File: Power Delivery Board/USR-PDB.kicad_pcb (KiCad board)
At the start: 2 copper layers, 110 x 150 mm, 40 parts, among them IC1 LM7805ECT, IC2 LM7805ECT, J1 XT90PW-M, U10 Anderson PP45 Vert. 2x1, U11 Anderson PP45 Vert. 2x1, U12 Anderson PP45 Vert. 2x1, U14 MCP3002-I/P, U17 AMS1117-3.3, U2 Anderson PP45 Vert. 2x1, U3 Anderson PP45 Vert. 2x1, U4 Anderson PP45 Vert. 2x1, U5 Anderson PP45 Vert. 2x1, U6 Anderson PP45 Vert. 2x1, U7 LM2676T-12_NOPB

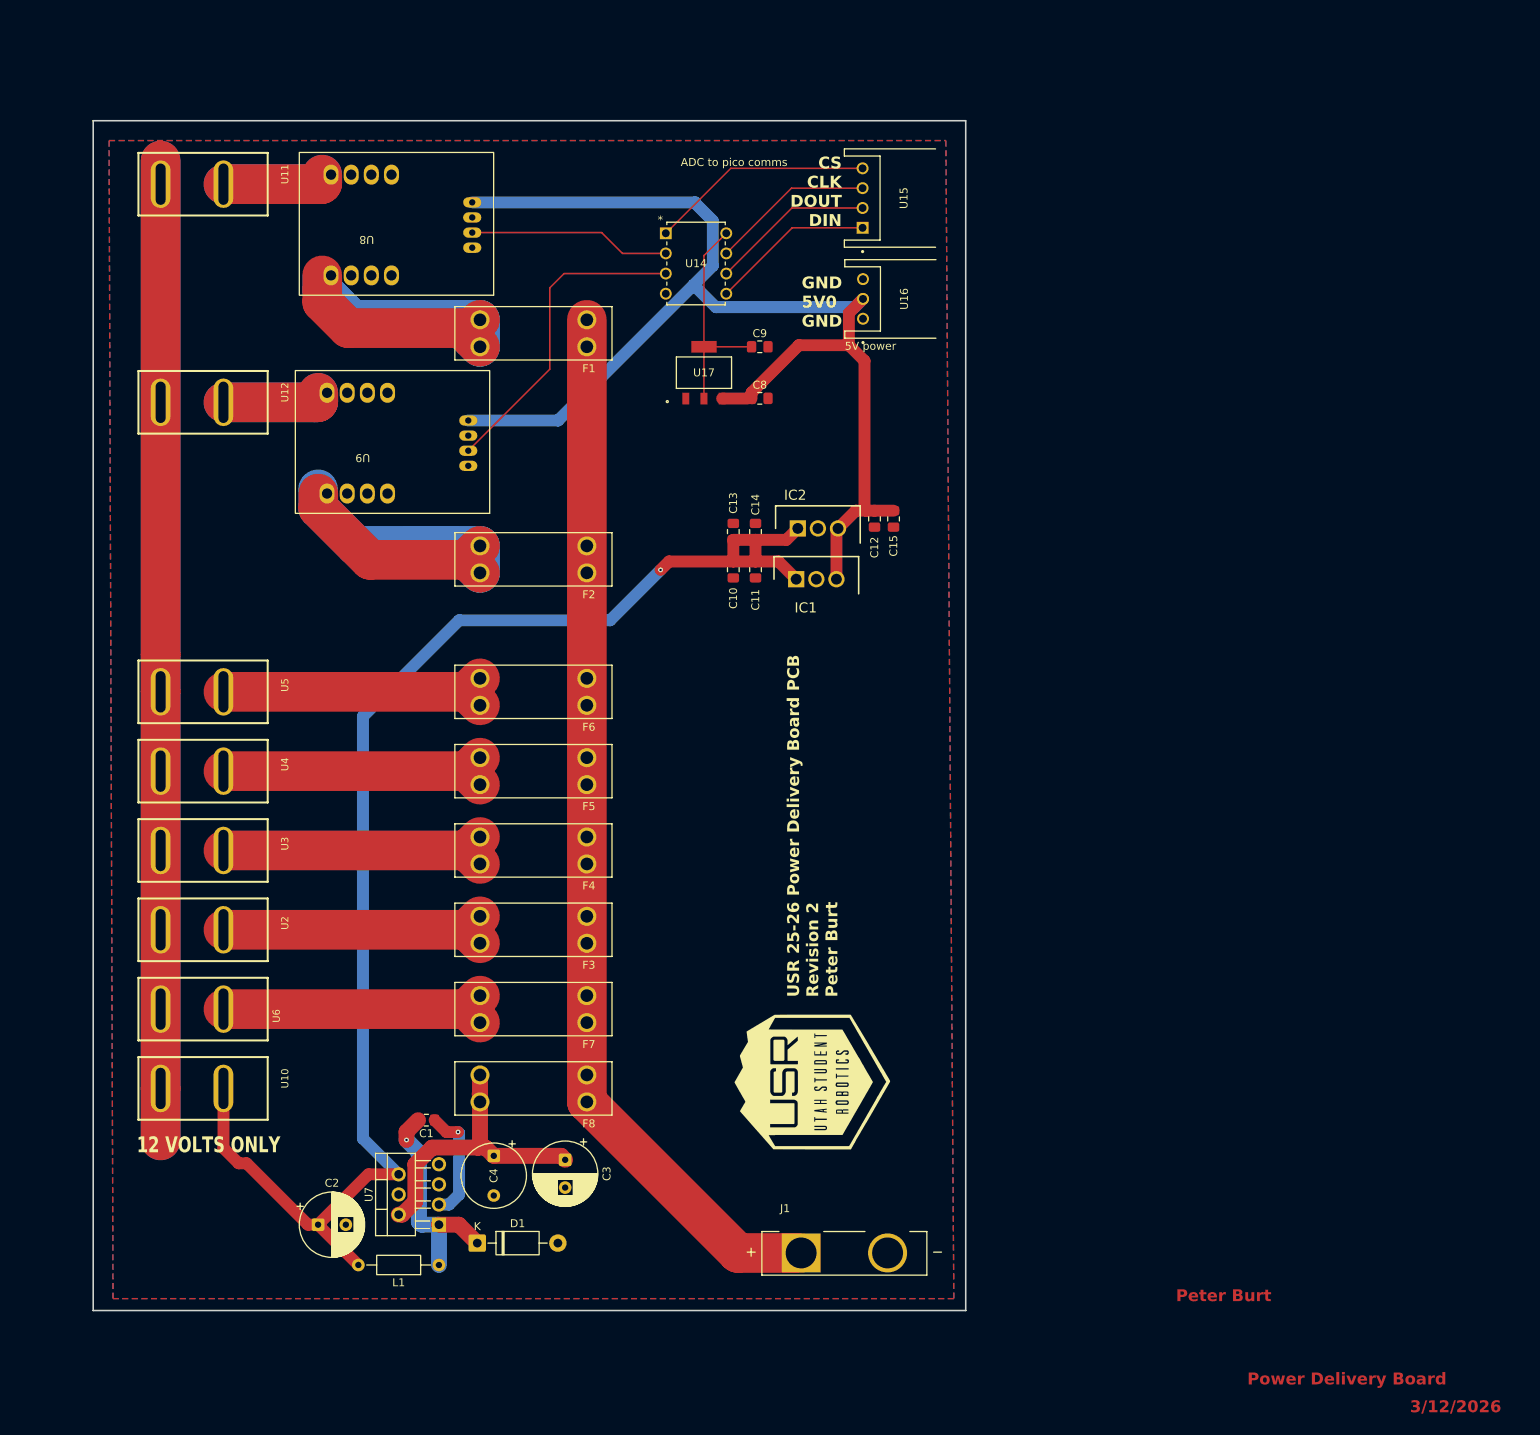
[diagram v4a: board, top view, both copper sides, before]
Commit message: updated trace widths for HE sensors
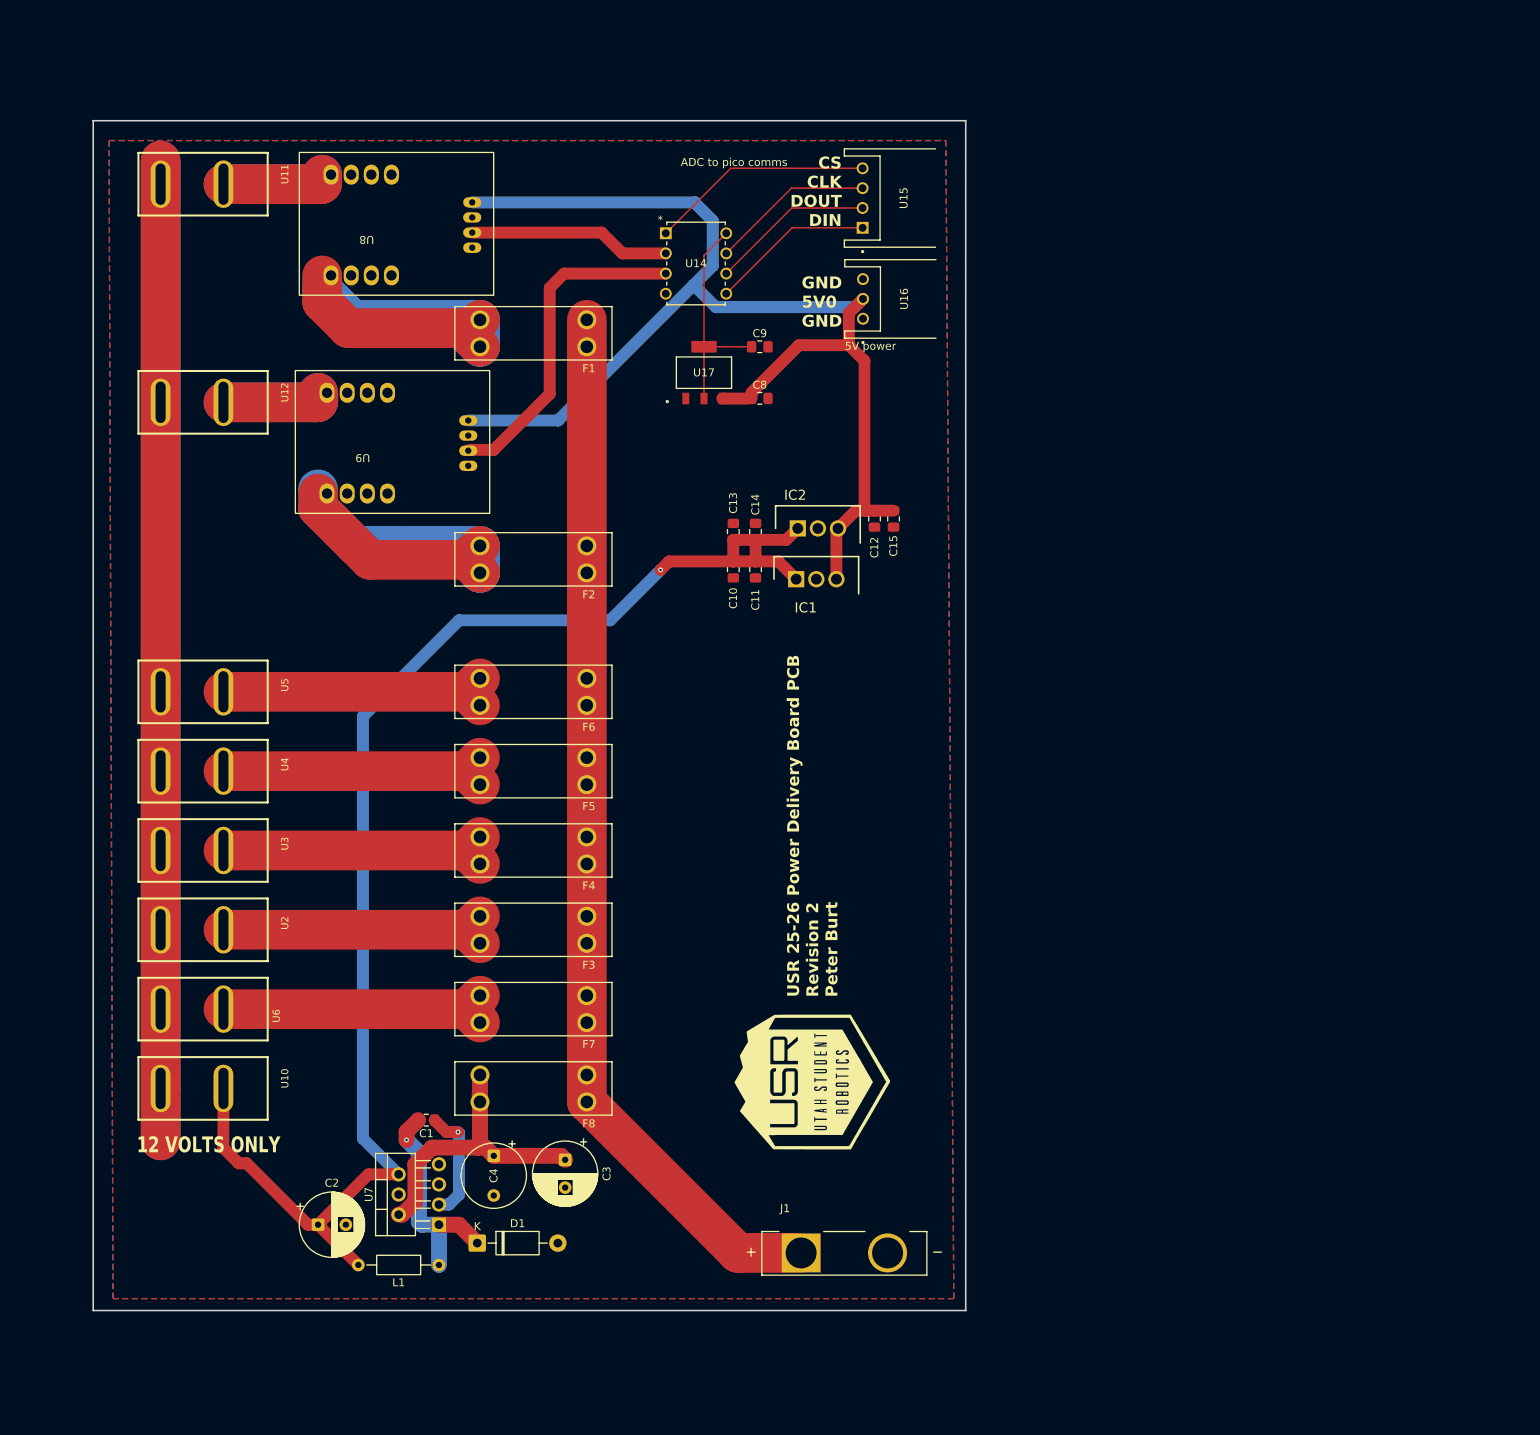
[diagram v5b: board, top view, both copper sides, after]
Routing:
- net HE2_out: track 40.2 -> 42.0 mm
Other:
- board text removed: "3/12/2026"
- board text removed: "Peter Burt"
- board text removed: "Power Delivery Board"
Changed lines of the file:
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@@
 	)
 	(paper "A4")
+	(title_block
+		(title "Power Delivery Board 2025-2026")
+		(date "2026-03-26")
+		(company "Utah Student Robotics")
+		(comment 1 "Peter Burt ")
+	)
 	(layers
 		(0 "F.Cu" signal)
@@
 		(layer "Edge.Cuts")
 	)
-	(gr_text "Peter Burt\n"
-		(at 178 180 0)
-		(layer "F.Cu")
-		(effects
-			(font
-				(size 1.5 1.5)
-				(thickness 0.3)
-				(bold yes)
-			)
-			(justify left bottom)
-		)
-	)
-	(gr_text "Power Delivery Board\n"
-		(at 187 190.5 0)
-		(layer "F.Cu")
-		(effects
-			(font
-				(size 1.5 1.5)
-				(thickness 0.3)
-				(bold yes)
-			)
-			(justify left bottom)
-		)
-	)
-	(gr_text "3/12/2026\n"
-		(at 207.5 194 0)
-		(layer "F.Cu")
-		(effects
-			(font
-				(size 1.5 1.5)
-				(thickness 0.3)
-				(bold yes)
-			)
-			(justify left bottom)
-		)
-	)
 	(gr_text "ADC to pico comms"
 		(at 115.57 36.83 0)
@@
 		(start 100.86 50.27)
 		(end 113.69 50.27)
-		(width 0.2)
+		(width 1.5)
 		(layer "F.Cu")
 		(net "HE2_out")
@@
 		(start 99.06 52.07)
 		(end 100.86 50.27)
-		(width 0.2)
+		(width 1.5)
 		(layer "F.Cu")
 		(net "HE2_out")
 	)
 	(segment
-		(start 88.785 72.6025)
-		(end 99.06 62.3275)
-		(width 0.2)
+		(start 88.8875 72.5)
+		(end 92 72.5)
+		(width 1.5)
 		(layer "F.Cu")
 		(net "HE2_out")
 	)
 	(segment
-		(start 99.06 62.3275)
+		(start 92 72.5)
+		(end 99.06 65.44)
+		(width 1.5)
+		(layer "F.Cu")
+		(net "HE2_out")
+	)
+	(segment
+		(start 99.06 65.44)
 		(end 99.06 52.07)
+		(width 1.5)
+		(layer "F.Cu")
+		(net "HE2_out")
+	)
+	(segment
+		(start 88.785 72.6025)
+		(end 88.8875 72.5)
 		(width 0.2)
 		(layer "F.Cu")
@@
 		(start 89.285 45.1025)
 		(end 105.6025 45.1025)
-		(width 0.2)
+		(width 1.5)
 		(layer "F.Cu")
 		(net "HE1_out")
@@
 		(start 108.23 47.73)
 		(end 113.69 47.73)
-		(width 0.2)
+		(width 1.5)
 		(layer "F.Cu")
 		(net "HE1_out")
@@
 		(start 105.6025 45.1025)
 		(end 108.23 47.73)
-		(width 0.2)
+		(width 1.5)
 		(layer "F.Cu")
 		(net "HE1_out")

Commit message: Added vias to PDB to stitch together front and back ground planes
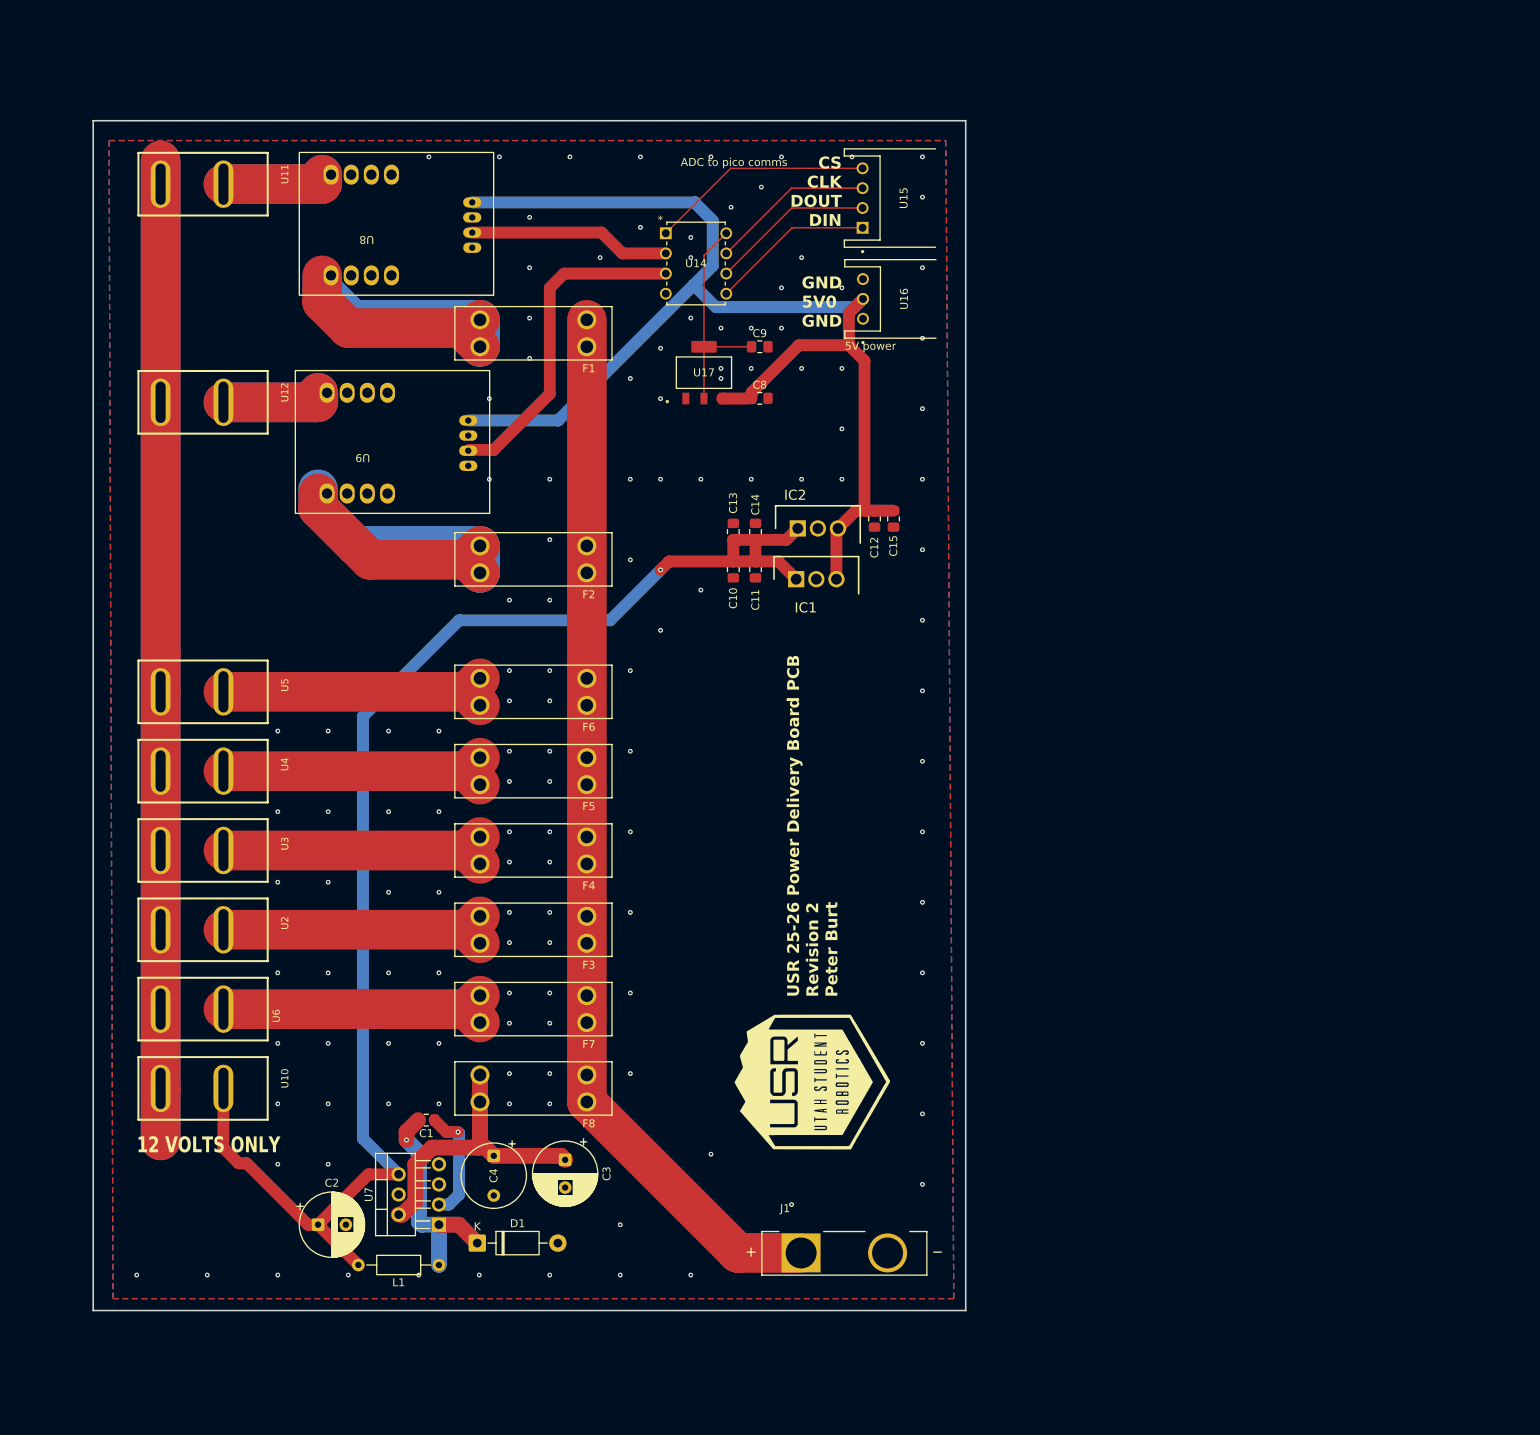
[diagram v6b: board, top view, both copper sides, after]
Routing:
- net GND: vias 0 -> 132

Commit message: generated gerbers for all remaining pcbs
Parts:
- added REF**: MountingHole_3.2mm_M3_DIN965_Pad_TopBottom, MountingHole:MountingHole_3.2mm_M3_DIN965_Pad_TopBottom, F.Cu at (132.1, 71.1)
- added REF**: MountingHole_3.2mm_M3_DIN965_Pad_TopBottom, MountingHole:MountingHole_3.2mm_M3_DIN965_Pad_TopBottom, F.Cu at (59.7, 53.3)
- added REF**: MountingHole_3.2mm_M3_DIN965_Pad_TopBottom, MountingHole:MountingHole_3.2mm_M3_DIN965_Pad_TopBottom, F.Cu at (49.5, 172.7)
- added REF**: MountingHole_3.2mm_M3_DIN965_Pad_TopBottom, MountingHole:MountingHole_3.2mm_M3_DIN965_Pad_TopBottom, F.Cu at (109.2, 172.7)

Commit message: Complete redesign of PDB pcb
AAAAAAAAAAAAAAAAAAAAAAAAAAAAAAAAAAAAAAAAAAAA
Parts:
- removed the REF** at (132.1, 71.1)
- removed the REF** at (59.7, 53.3)
- removed the REF** at (49.5, 172.7)
- removed the REF** at (109.2, 172.7)
- added G***: LOGO, LOGO, F.Cu at (104.1, 40.6)
- added REF**: MountingHole_3.2mm_M3_Pad_Via, MountingHole:MountingHole_3.2mm_M3_Pad_Via, F.Cu at (37.0, 23.0)
- added REF**: MountingHole_3.2mm_M3_Pad_Via, MountingHole:MountingHole_3.2mm_M3_Pad_Via, F.Cu at (115.4, 181.5)
- added REF**: MountingHole_3.2mm_M3_Pad_Via, MountingHole:MountingHole_3.2mm_M3_Pad_Via, F.Cu at (37.0, 181.5)
- added REF**: MountingHole_3.2mm_M3_Pad_Via, MountingHole:MountingHole_3.2mm_M3_Pad_Via, F.Cu at (115.4, 23.0)
- C1, C10, C11, C12, C13, C14, C15, C8, C9, U17: moved to B.Cu
- C4: footprint Capacitor_THT:CP_Radial_Tantal_D8.0mm_P5.00mm -> Capacitor_THT:CP_Radial_D10.0mm_P5.00mm
- moved J1 159.8 mm to (77.5, 25.4), turned to 180 degrees
- moved U16 137.7 mm to (37.1, 140.0), turned to -90 degrees
- moved C15 126.6 mm to (36.8, 151.1), turned to 180 degrees
- moved C14 118.0 mm to (36.8, 161.3), turned to 180 degrees
- moved C12 114.3 mm to (49.5, 151.1), turned to 0 degrees
- moved C13 114.3 mm to (36.8, 158.8), turned to 180 degrees
- moved IC1 114.2 mm to (39.9, 158.7), turned to 90 degrees
- moved IC2 114.0 mm to (45.7, 158.7), turned to 90 degrees
- moved U15 106.8 mm to (37.5, 38.0), turned to -90 degrees
- moved C11 103.7 mm to (49.5, 158.8), turned to 0 degrees
- moved C10 103.5 mm to (49.5, 161.3), turned to 0 degrees
- moved C8 78.3 mm to (48.3, 53.1), turned to -90 degrees
- moved C9 70.4 mm to (57.1, 42.9), turned to -90 degrees
- moved U17 66.6 mm to (53.3, 48.8), turned to 180 degrees
- moved U14 52.8 mm to (61.0, 41.9), turned to 180 degrees
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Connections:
- U8 pad 3: unconnected-(U8-in_2-Pad3) -> HE_sensor1
- U8 pad 4: unconnected-(U8-in_3-Pad4) -> HE_sensor1
- U8 pad 5: unconnected-(U8-in_4-Pad5) -> HE_sensor1
- U8 pad 6: unconnected-(U8-out_4-Pad6) -> Net-(U11-VCC)
- U8 pad 7: unconnected-(U8-out_3-Pad7) -> Net-(U11-VCC)
- U8 pad 8: unconnected-(U8-out_2-Pad8) -> Net-(U11-VCC)
- U9 pad 3: unconnected-(U9-in_2-Pad3) -> HE_sensor2
- U9 pad 4: unconnected-(U9-in_3-Pad4) -> HE_sensor2
- U9 pad 5: unconnected-(U9-in_4-Pad5) -> HE_sensor2
- U9 pad 6: unconnected-(U9-out_4-Pad6) -> Net-(U12-VCC)
- U9 pad 7: unconnected-(U9-out_3-Pad7) -> Net-(U12-VCC)
- U9 pad 8: unconnected-(U9-out_2-Pad8) -> Net-(U12-VCC)
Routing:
- net GND: track 247.0 -> 0.00 mm, vias 132 -> 0
- net Vin: track 133.3 -> 0.00 mm
- net 5V_OUT: track 160.8 -> 241.0 mm, vias 0 -> 1
- net 12V_OUT: track 180.8 -> 101.0 mm, vias 1 -> 0
- net HE_sensor2: track 66.6 -> 27.2 mm
- net HE_sensor1: track 59.5 -> 27.2 mm
- net Net-(U2-VCC): track 38.9 -> 17.8 mm
- net Net-(U5-VCC): track 35.9 -> 17.8 mm
- net Net-(U4-VCC): track 35.9 -> 17.8 mm
- net Net-(U3-VCC): track 35.5 -> 17.8 mm
- net Net-(U6-VCC): track 35.5 -> 17.8 mm
- net HE1_out: track 25.5 -> 11.4 mm
- net 3.3V_out: track 28.0 -> 14.0 mm
- net Net-(U7-BOOST): track 14.6 -> 2.45 mm, vias 1 -> 0
- net Din: track 20.6 -> 10.2 mm
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- added copper zone on F.Cu, net Vin
- removed copper zone on F.Cu, net GND
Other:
- board size 110 x 150 mm -> 86.1 x 166.1 mm
- board text added: "DIN DOUT CLK CS"
- board text added: "USR 25-26 Power Delivery Board PCB Revision 3 Peter Burt Vincent Banh"
- board text removed: "CS CLK DOUT DIN"
- board text removed: "USR 25-26 Power Delivery Board PCB Revision 2 Peter Burt"
